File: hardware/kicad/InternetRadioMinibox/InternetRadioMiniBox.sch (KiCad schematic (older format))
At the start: 51 parts, among them IC1 ESP8266, IC2 ATMEGA328P-P, IC3 23K256, IC4 VS1011e, IC5 LM386, M1 TSR1-2433, M2 TSR1-2433, M3 TSR1-2433, P1 CONN_01X02, P2 CONN_01X03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

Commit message: Changed connection to variable capacitor.
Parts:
- removed P2: CONN_01X03, Connect:PINHEAD1-3, symbol CONN_01X03
- added P?: CONN_01X02, symbol CONN_01X02
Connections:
- wire segments 217 -> 256
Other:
- note added: "To 0-135pF Rotary \nVariable Capacitor."
- note removed: "To 0-135pF Rotary \nVariable Capacitor. \nCase connected \nto ground."
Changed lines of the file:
@@
 $EndComp
 Text Notes 15350 2950 0    39   ~ 0
-To 0-135pF Rotary \nVariable Capacitor. \nCase connected \nto ground.
+To 0-135pF Rotary \nVariable Capacitor.
 $Comp
 L GND #PWR013
@@
 $EndComp
 $Comp
-L CONN_01X03 P2
-U 1 1 58D6D6E2
-P 15550 3300
-F 0 "P2" H 15550 3500 50  0000 C CNN
-F 1 "CONN_01X03" V 15650 3300 50  0000 C CNN
-F 2 "Connect:PINHEAD1-3" H 15550 3300 50  0001 C CNN
-F 3 "" H 15550 3300 50  0000 C CNN
-	1    15550 3300
-	1    0    0    -1
-$EndComp
-$Comp
 L CONN_01X02 P3
 U 1 1 58D7596B
@@
 	4400 2800 5300 2800
 Wire Wire Line
-	1350 8300 2800 8300
+	1350 8300 2400 8300
+Wire Wire Line
+	2400 8300 2800 8300
 Wire Wire Line
 	3300 8600 3300 8700
@@
 	6750 2200 4400 2200
 Wire Wire Line
-	6550 8500 8200 8500
+	6550 8500 7750 8500
+Wire Wire Line
+	7750 8500 8200 8500
 Wire Wire Line
 	6550 8500 6550 2500
@@
 	6350 3000 6350 8400
 Wire Wire Line
-	4400 2400 5900 2400
+	4400 2400 4500 2400
+Wire Wire Line
+	4500 2400 5900 2400
 Wire Wire Line
 	4500 4500 4500 2400
 Wire Wire Line
-	3500 4500 4500 4500
+	3500 4500 3600 4500
+Wire Wire Line
+	3600 4500 4500 4500
 Wire Wire Line
 	3500 4500 3500 4600
 Connection ~ 4500 2400
 Wire Wire Line
-	3500 5100 3500 5500
-Wire Wire Line
-	2350 1450 2350 4600
-Wire Wire Line
-	2350 5100 2350 5500
+	3500 5100 3500 5150
+Wire Wire Line
+	3500 5150 3500 5500
+Wire Wire Line
+	2350 1450 2350 2600
+Wire Wire Line
+	2350 2600 2350 4500
+Wire Wire Line
+	2350 4500 2350 4600
+Wire Wire Line
+	2350 5100 2350 5150
+Wire Wire Line
+	2350 5150 2350 5500
 Wire Wire Line
 	10200 2200 12350 2200
 Wire Wire Line
-	12350 2200 12350 2450
+	12350 2200 12350 2400
+Wire Wire Line
+	12350 2400 12350 2450
 Wire Wire Line
 	12350 2400 12200 2400
@@
 	11700 2400 11900 2400
 Wire Wire Line
-	11700 2300 11700 2450
+	11700 2300 11700 2400
+Wire Wire Line
+	11700 2400 11700 2450
 Connection ~ 11700 2400
 Connection ~ 12350 2400
@@
 	12350 2750 12350 2750
 Wire Wire Line
-	7600 950  7600 2550
+	7600 950  7600 1100
+Wire Wire Line
+	7600 1100 7600 1600
+Wire Wire Line
+	7600 1600 7600 2550
 Wire Wire Line
 	8300 3900 7600 3900
 Wire Wire Line
-	7600 2850 7600 4100
+	7600 2850 7600 3900
+Wire Wire Line
+	7600 3900 7600 4100
 Connection ~ 7600 3900
 Wire Wire Line
 	8300 3800 8050 3800
 Wire Wire Line
-	8050 2850 8050 4100
-Wire Wire Line
-	8050 1100 8050 2550
+	8050 2850 8050 3800
+Wire Wire Line
+	8050 3800 8050 4100
+Wire Wire Line
+	8050 1100 8050 1900
+Wire Wire Line
+	8050 1900 8050 2550
 Connection ~ 8050 3800
 Wire Wire Line
 	10400 1500 10400 3050
 Wire Wire Line
-	10200 3050 10950 3050
+	10200 3050 10400 3050
+Wire Wire Line
+	10400 3050 10950 3050
 Wire Wire Line
 	10200 2300 11700 2300
@@
 	11250 2950 11250 3300
 Wire Wire Line
-	11250 3300 15350 3300
+	11250 3300 15050 3300
+Wire Wire Line
+	15050 3300 15350 3300
 Wire Wire Line
 	10200 2850 11350 2850
@@
 	10200 3500 10950 3500
 Wire Wire Line
-	11550 3500 11550 4100
+	11550 3500 11550 3800
+Wire Wire Line
+	11550 3800 11550 4100
 Connection ~ 11550 3800
 Connection ~ 10400 3050
@@
 	4400 2300 6100 2300
 Wire Bus Line
-	1150 6300 14650 6300
+	1150 6300 1250 6300
+Wire Bus Line
+	1250 6300 1400 6300
+Wire Bus Line
+	1400 6300 1550 6300
+Wire Bus Line
+	1550 6300 1700 6300
+Wire Bus Line
+	1700 6300 5200 6300
+Wire Bus Line
+	5200 6300 5400 6300
+Wire Bus Line
+	5400 6300 5600 6300
+Wire Bus Line
+	5600 6300 5800 6300
+Wire Bus Line
+	5800 6300 6000 6300
+Wire Bus Line
+	6000 6300 6200 6300
+Wire Bus Line
+	6200 6300 7250 6300
+Wire Bus Line
+	7250 6300 7350 6300
+Wire Bus Line
+	7350 6300 7450 6300
+Wire Bus Line
+	7450 6300 7550 6300
+Wire Bus Line
+	7550 6300 13100 6300
+Wire Bus Line
+	13100 6300 13300 6300
+Wire Bus Line
+	13300 6300 13500 6300
+Wire Bus Line
+	13500 6300 13700 6300
+Wire Bus Line
+	13700 6300 14650 6300
 Wire Wire Line
 	5100 2900 5100 6200
@@
 Wire Wire Line
 	1800 8000 1800 6400
-Connection ~ 15050 3700
 Wire Bus Line
 	13100 6300 13050 6300
@@
 Connection ~ 2700 7050
 Wire Wire Line
-	2400 7050 3300 7050
+	2400 7050 2700 7050
+Wire Wire Line
+	2700 7050 3300 7050
 Wire Wire Line
 	3700 3600 3700 3550
 Wire Wire Line
-	3300 7000 3300 7550
+	3300 7000 3300 7050
+Wire Wire Line
+	3300 7050 3300 7550
 Wire Wire Line
 	8050 1900 8300 1900
 Wire Wire Line
-	7600 1100 10400 1100
+	7600 1100 8050 1100
+Wire Wire Line
+	8050 1100 10400 1100
 Connection ~ 7600 1100
 Connection ~ 8050 1100
@@
 	8600 9400 8600 9500
 Wire Wire Line
-	8600 9500 8800 9500
-Wire Wire Line
-	8700 9400 8700 9600
+	8600 9500 8700 9500
+Wire Wire Line
+	8700 9500 8800 9500
+Wire Wire Line
+	8700 9400 8700 9500
+Wire Wire Line
+	8700 9500 8700 9600
 Wire Wire Line
 	8800 9500 8800 9400
@@
 	8950 9400 8950 9500
 Wire Wire Line
-	8950 9500 9150 9500
-Wire Wire Line
-	9050 9400 9050 9600
+	8950 9500 9050 9500
+Wire Wire Line
+	9050 9500 9150 9500
+Wire Wire Line
+	9050 9400 9050 9500
+Wire Wire Line
+	9050 9500 9050 9600
 Connection ~ 9050 9500
 Wire Wire Line
@@
 	8600 7200 8600 7100
 Wire Wire Line
-	8600 7100 8800 7100
-Wire Wire Line
-	8700 6450 8700 7200
+	8600 7100 8700 7100
+Wire Wire Line
+	8700 7100 8800 7100
+Wire Wire Line
+	8700 6450 8700 7100
+Wire Wire Line
+	8700 7100 8700 7200
 Connection ~ 8700 7100
 Wire Wire Line
@@
 	6250 10700 6250 10800
 Wire Wire Line
-	9050 6450 9050 7200
+	9050 6450 9050 7100
+Wire Wire Line
+	9050 7100 9050 7200
 Wire Wire Line
 	8950 7200 8950 7100
@@
 	10200 7150 10200 7350
 Wire Wire Line
-	10150 7150 10400 7150
-Wire Wire Line
-	10750 7150 10750 7950
+	10150 7150 10200 7150
+Wire Wire Line
+	10200 7150 10400 7150
+Wire Wire Line
+	10750 7150 10750 7850
+Wire Wire Line
+	10750 7850 10750 7950
 Wire Wire Line
 	10200 7850 10200 7650
@@
 	10000 9200 10000 9250
 Wire Wire Line
-	10000 9250 10600 9250
-Wire Wire Line
-	10200 9200 10200 9300
+	10000 9250 10200 9250
+Wire Wire Line
+	10200 9250 10400 9250
+Wire Wire Line
+	10400 9250 10600 9250
+Wire Wire Line
+	10200 9200 10200 9250
+Wire Wire Line
+	10200 9250 10200 9300
 Connection ~ 10200 9250
 Wire Wire Line
@@
 	2850 10150 2650 10150
 Wire Wire Line
-	1150 10150 1450 10150
-Wire Wire Line
-	2050 10700 2050 10800
+	1150 10150 1400 10150
+Wire Wire Line
+	1400 10150 1450 10150
+Wire Wire Line
+	2050 10700 2050 10750
+Wire Wire Line
+	2050 10750 2050 10800
 Wire Wire Line
 	3250 10150 3350 10150
@@
 Connection ~ 2350 2600
 Wire Wire Line
-	13400 8500 13400 8650
+	13400 8500 13400 8600
+Wire Wire Line
+	13400 8600 13400 8650
 Wire Wire Line
 	13200 8300 13200 8600
@@
 	13400 7650 13400 7900
 Wire Wire Line
-	13800 8200 14100 8200
+	13800 8200 14000 8200
+Wire Wire Line
+	14000 8200 14100 8200
 Wire Wire Line
 	14000 8500 14000 8200
@@
 	14000 9100 14000 9150
 Wire Wire Line
-	13000 8100 13200 8100
-Wire Wire Line
-	13050 8100 13050 8600
+	13000 8100 13050 8100
+Wire Wire Line
+	13050 8100 13200 8100
+Wire Wire Line
+	13050 8100 13050 8450
+Wire Wire Line
+	13050 8450 13050 8600
 Connection ~ 13050 8100
 Connection ~ 13050 8450
@@
 	10700 7150 10750 7150
 Wire Wire Line
-	9650 7850 10400 7850
+	9650 7850 10200 7850
+Wire Wire Line
+	10200 7850 10400 7850
 Connection ~ 10200 7850
 Wire Wire Line
@@
 ISP for AVR (Optional)
 Wire Wire Line
-	15350 3400 15350 3700
-Wire Wire Line
-	15350 3700 15050 3700
-Wire Wire Line
-	15050 3650 15050 3800
+	15050 3650 15050 3700
+Wire Wire Line
+	15050 3700 15050 3800
 Text Notes 3950 1750 0    60   ~ 0
 Main Processor
@@
 ESP8266 Board has 12K pullups \non GPIO0 and CHIP-EN
 NoConn ~ 3000 2700
+$Comp
+L CONN_01X02 P?
+U 1 1 58F755C2
+P 15550 3250
+F 0 "P?" H 15550 3400 50  0000 C CNN
+F 1 "CONN_01X02" V 15650 3250 50  0000 C CNN
+F 2 "" H 15550 3250 50  0000 C CNN
+F 3 "" H 15550 3250 50  0000 C CNN
+	1    15550 3250
+	1    0    0    -1
+$EndComp
 $EndSCHEMATC

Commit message: Small changes to the schematic.
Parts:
- C13: footprint (none) -> Capacitors_SMD:C_0805_HandSoldering
- R17, R18, R19, R20: footprint (none) -> Resistors_SMD:R_0805_HandSoldering
- gave numbers to parts that had none: 2
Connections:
- wire segments 256 -> 215
- no-connect marks 18 -> 19

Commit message: KiCAD update of library caches.
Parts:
- D1, D2: symbol LED -> LED-RESCUE-InternetRadioMiniBox
- IC5: symbol LM386 -> LM386-RESCUE-InternetRadioMiniBox
- SW1, SW2: symbol SW_PUSH_SMALL -> SW_PUSH_SMALL-RESCUE-InternetRadioMiniBox
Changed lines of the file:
@@
 $EndComp
 $Comp
-L LED D2
+L LED-RESCUE-InternetRadioMiniBox D2
 U 1 1 58AB9582
 P 11100 3800
@@
 $EndComp
 $Comp
-L LED D1
+L LED-RESCUE-InternetRadioMiniBox D1
 U 1 1 58AB95F9
 P 11100 3500
@@
 $EndComp
 $Comp
-L SW_PUSH_SMALL SW1
+L SW_PUSH_SMALL-RESCUE-InternetRadioMiniBox SW1
 U 1 1 58CEFEA7
 P 2400 4850
@@
 $EndComp
 $Comp
-L SW_PUSH_SMALL SW2
+L SW_PUSH_SMALL-RESCUE-InternetRadioMiniBox SW2
 U 1 1 58CF00A3
 P 3550 4850
@@
 $EndComp
 $Comp
-L LM386 IC5
+L LM386-RESCUE-InternetRadioMiniBox IC5
 U 1 1 58D2B6DF
 P 13500 8200

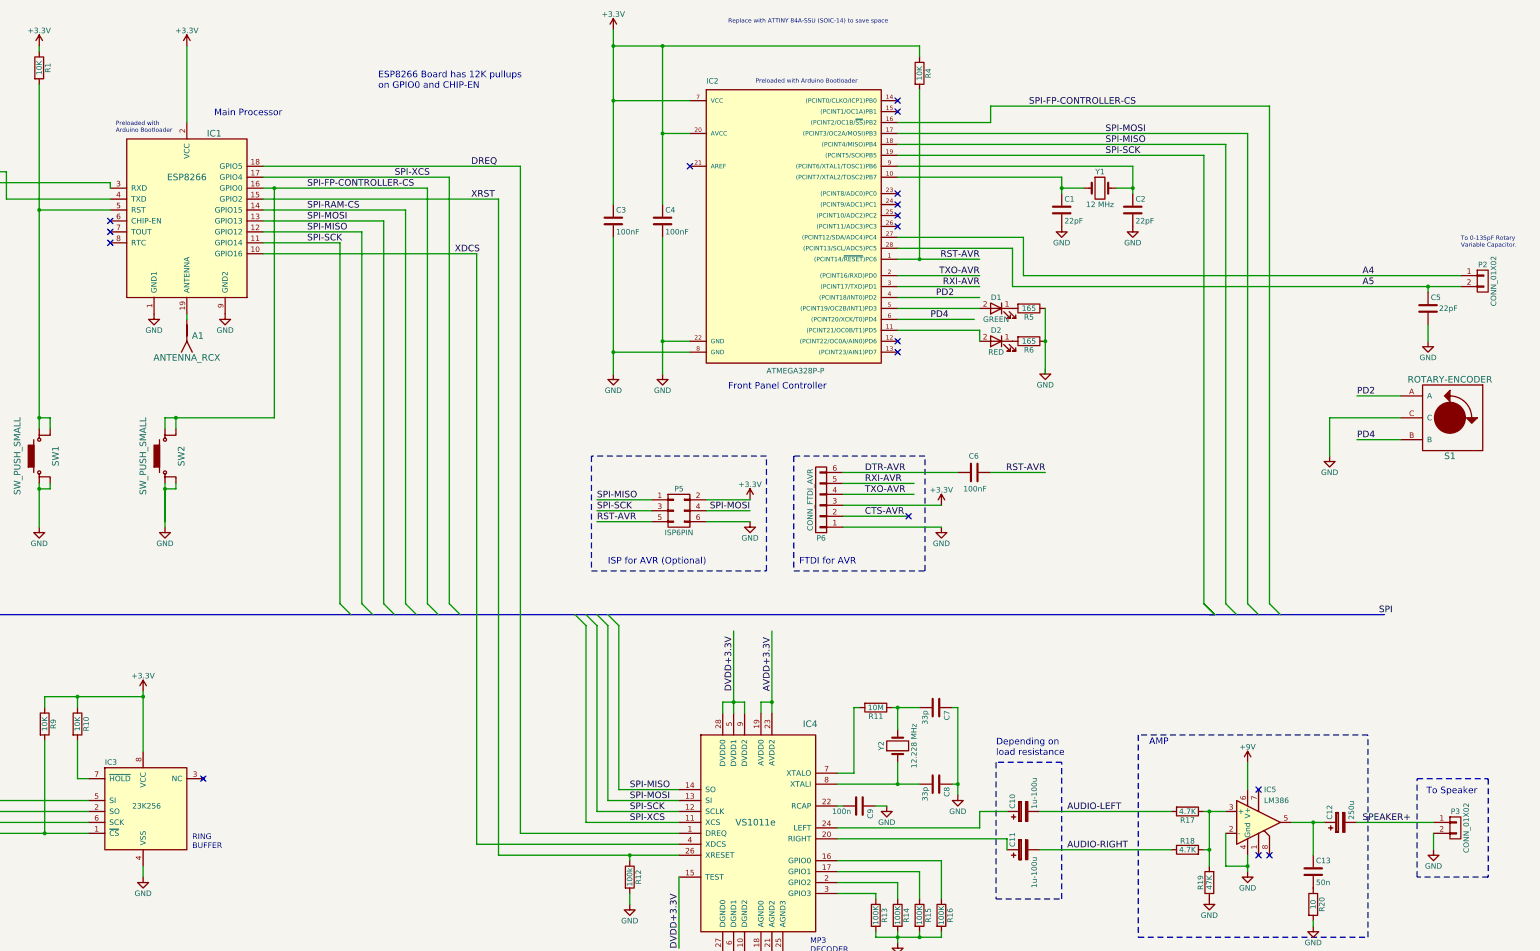
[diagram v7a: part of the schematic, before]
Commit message: Added decoupling capacitors.
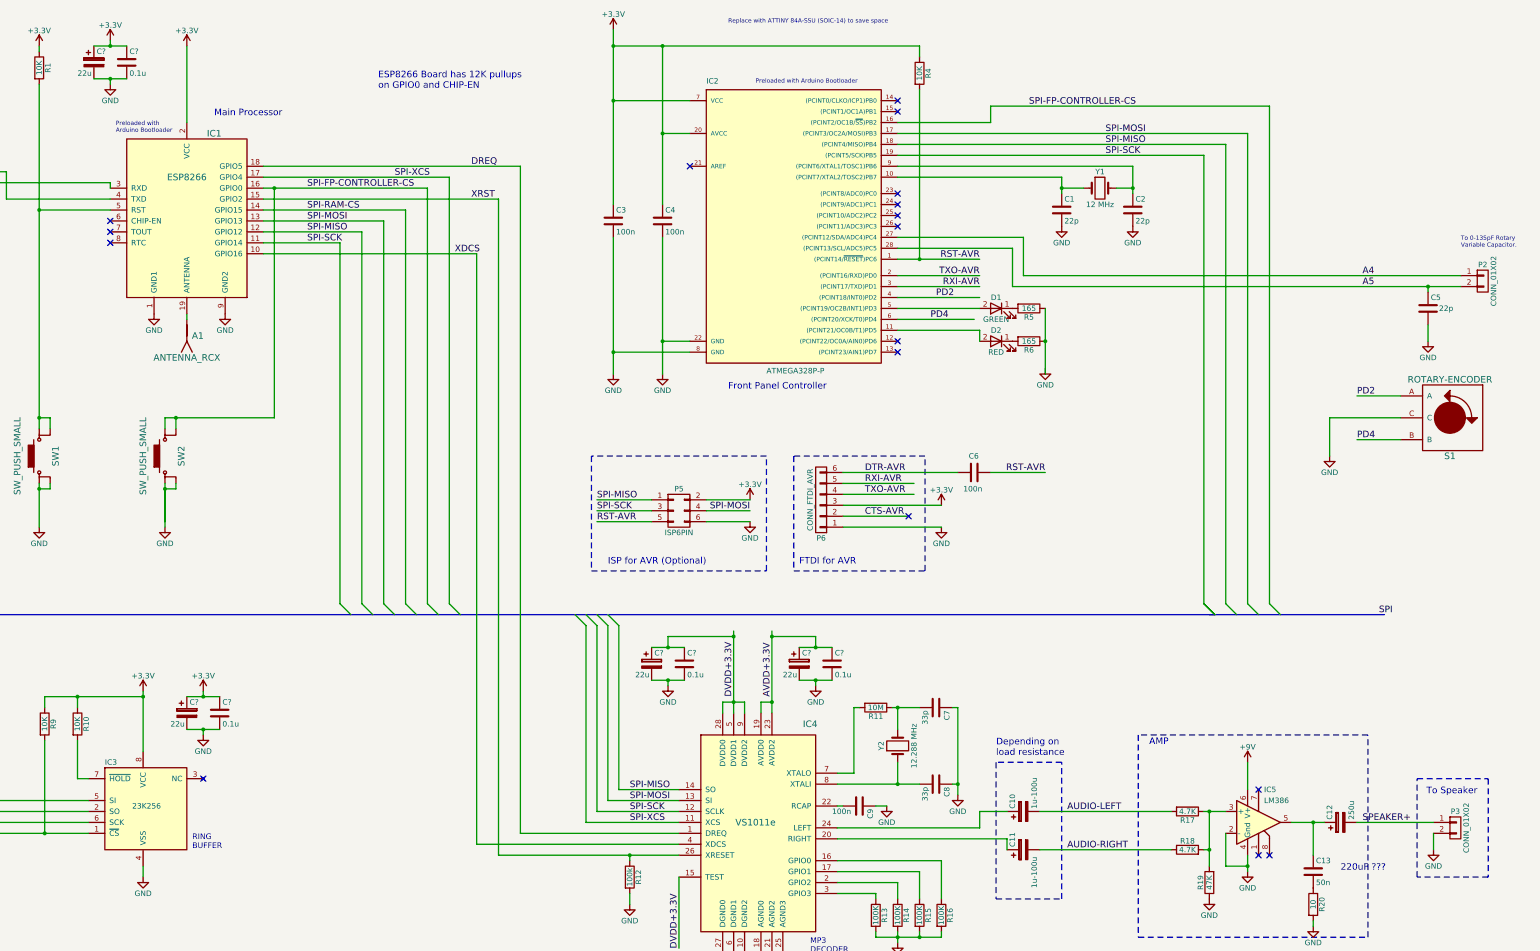
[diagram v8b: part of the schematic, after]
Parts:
- added C? (x4): 22u, symbol CP
- added C? (x4): 0.1u, symbol C
- C1, C2, C5: value 22pF -> 22p
- C3, C4, C6: value 100nF -> 100n
- Y2: value 12.228 MHz -> 12.288 MHz
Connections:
- wire segments 215 -> 233
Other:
- note added: "220uF ???"
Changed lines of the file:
@@
 P 11700 2600
 F 0 "C1" H 11725 2700 50  0000 L CNN
-F 1 "22pF" H 11725 2500 50  0000 L CNN
+F 1 "22p" H 11725 2500 50  0000 L CNN
 F 2 "Capacitors_SMD:C_0805_HandSoldering" H 11738 2450 50  0001 C CNN
 F 3 "" H 11700 2600 50  0000 C CNN
@@
 P 12350 2600
 F 0 "C2" H 12375 2700 50  0000 L CNN
-F 1 "22pF" H 12375 2500 50  0000 L CNN
+F 1 "22p" H 12375 2500 50  0000 L CNN
 F 2 "Capacitors_SMD:C_0805_HandSoldering" H 12388 2450 50  0001 C CNN
 F 3 "" H 12350 2600 50  0000 C CNN
@@
 P 7600 2700
 F 0 "C3" H 7625 2800 50  0000 L CNN
-F 1 "100nF" H 7625 2600 50  0000 L CNN
+F 1 "100n" H 7625 2600 50  0000 L CNN
 F 2 "Capacitors_SMD:C_0805_HandSoldering" H 7638 2550 50  0001 C CNN
 F 3 "" H 7600 2700 50  0000 C CNN
@@
 P 8050 2700
 F 0 "C4" H 8075 2800 50  0000 L CNN
-F 1 "100nF" H 8075 2600 50  0000 L CNN
+F 1 "100n" H 8075 2600 50  0000 L CNN
 F 2 "Capacitors_SMD:C_0805_HandSoldering" H 8088 2550 50  0001 C CNN
 F 3 "" H 8050 2700 50  0000 C CNN
@@
 P 15050 3500
 F 0 "C5" H 15075 3600 50  0000 L CNN
-F 1 "22pF" H 15150 3500 50  0000 L CNN
+F 1 "22p" H 15150 3500 50  0000 L CNN
 F 2 "Capacitors_SMD:C_0805_HandSoldering" H 15088 3350 50  0001 C CNN
 F 3 "" H 15050 3500 50  0000 C CNN
@@
 P 10900 5000
 F 0 "C6" V 10750 4950 50  0000 L CNN
-F 1 "100nF" V 11050 4900 50  0000 L CNN
+F 1 "100n" V 11050 4900 50  0000 L CNN
 F 2 "Capacitors_SMD:C_0805_HandSoldering" H 10938 4850 50  0001 C CNN
 F 3 "" H 10900 5000 50  0000 C CNN
@@
 P 10200 7500
 F 0 "Y2" H 10200 7650 50  0000 C CNN
-F 1 "12.228 MHz" H 10200 7350 50  0000 C CNN
+F 1 "12.288 MHz" H 10200 7350 50  0000 C CNN
 F 2 "" H 10200 7500 50  0001 C CNN
 F 3 "" H 10200 7500 50  0000 C CNN
@@
 Wire Wire Line
 	1300 2650 1800 2650
-Text Label 8700 7000 1    60   ~ 0
+Text Label 8700 7050 1    60   ~ 0
 DVDD+3.3V
-Text Label 9050 7000 1    60   ~ 0
+Text Label 9050 7050 1    60   ~ 0
 AVDD+3.3V
 Text Label 7500 10150 2    60   ~ 0
@@
 $EndComp
 NoConn ~ 10200 2450
+Text Notes 14250 8650 0    60   ~ 0
+220uF ???
+$Comp
+L CP C?
+U 1 1 5905CE91
+P 2850 1250
+F 0 "C?" H 2875 1350 50  0000 L CNN
+F 1 "22u" H 2700 1150 50  0000 L CNN
+F 2 "" H 2888 1100 50  0000 C CNN
+F 3 "" H 2850 1250 50  0000 C CNN
+	1    2850 1250
+	1    0    0    -1
+$EndComp
+$Comp
+L C C?
+U 1 1 5905CF1A
+P 3150 1250
+F 0 "C?" H 3175 1350 50  0000 L CNN
+F 1 "0.1u" H 3175 1150 50  0000 L CNN
+F 2 "" H 3188 1100 50  0000 C CNN
+F 3 "" H 3150 1250 50  0000 C CNN
+	1    3150 1250
+	1    0    0    -1
+$EndComp
+Wire Wire Line
+	2850 1100 3150 1100
+Wire Wire Line
+	2850 1400 3150 1400
+$Comp
+L +3.3V #PWR?
+U 1 1 5905E727
+P 3000 1050
+F 0 "#PWR?" H 3000 900 50  0001 C CNN
+F 1 "+3.3V" H 3000 1190 50  0000 C CNN
+F 2 "" H 3000 1050 50  0000 C CNN
+F 3 "" H 3000 1050 50  0000 C CNN
+	1    3000 1050
+	1    0    0    -1
+$EndComp
+$Comp
+L GND #PWR?
+U 1 1 5905E7A5
+P 3000 1450
+F 0 "#PWR?" H 3000 1200 50  0001 C CNN
+F 1 "GND" H 3000 1300 50  0000 C CNN
+F 2 "" H 3000 1450 50  0000 C CNN
+F 3 "" H 3000 1450 50  0000 C CNN
+	1    3000 1450
+	1    0    0    -1
+$EndComp
+Wire Wire Line
+	3000 1050 3000 1100
+Connection ~ 3000 1100
+Wire Wire Line
+	3000 1450 3000 1400
+Connection ~ 3000 1400
+$Comp
+L CP C?
+U 1 1 59060BA4
+P 3700 7200
+F 0 "C?" H 3725 7300 50  0000 L CNN
+F 1 "22u" H 3550 7100 50  0000 L CNN
+F 2 "" H 3738 7050 50  0000 C CNN
+F 3 "" H 3700 7200 50  0000 C CNN
+	1    3700 7200
+	1    0    0    -1
+$EndComp
+$Comp
+L C C?
+U 1 1 59060BAA
+P 4000 7200
+F 0 "C?" H 4025 7300 50  0000 L CNN
+F 1 "0.1u" H 4025 7100 50  0000 L CNN
+F 2 "" H 4038 7050 50  0000 C CNN
+F 3 "" H 4000 7200 50  0000 C CNN
+	1    4000 7200
+	1    0    0    -1
+$EndComp
+Wire Wire Line
+	3700 7050 4000 7050
+Wire Wire Line
+	3700 7350 4000 7350
+$Comp
+L +3.3V #PWR?
+U 1 1 59060BB4
+P 3850 7000
+F 0 "#PWR?" H 3850 6850 50  0001 C CNN
+F 1 "+3.3V" H 3850 7140 50  0000 C CNN
+F 2 "" H 3850 7000 50  0000 C CNN
+F 3 "" H 3850 7000 50  0000 C CNN
+	1    3850 7000
+	1    0    0    -1
+$EndComp
+$Comp
+L GND #PWR?
+U 1 1 59060BBA
+P 3850 7400
+F 0 "#PWR?" H 3850 7150 50  0001 C CNN
+F 1 "GND" H 3850 7250 50  0000 C CNN
+F 2 "" H 3850 7400 50  0000 C CNN
+F 3 "" H 3850 7400 50  0000 C CNN
+	1    3850 7400
+	1    0    0    -1
+$EndComp
+Wire Wire Line
+	3850 7000 3850 7050
+Connection ~ 3850 7050
+Wire Wire Line
+	3850 7400 3850 7350
+Connection ~ 3850 7350
+$Comp
+L CP C?
+U 1 1 59062737
+P 7950 6750
+F 0 "C?" H 7975 6850 50  0000 L CNN
+F 1 "22u" H 7800 6650 50  0000 L CNN
+F 2 "" H 7988 6600 50  0000 C CNN
+F 3 "" H 7950 6750 50  0000 C CNN
+	1    7950 6750
+	1    0    0    -1
+$EndComp
+$Comp
+L C C?
+U 1 1 5906273D
+P 8250 6750
+F 0 "C?" H 8275 6850 50  0000 L CNN
+F 1 "0.1u" H 8275 6650 50  0000 L CNN
+F 2 "" H 8288 6600 50  0000 C CNN
+F 3 "" H 8250 6750 50  0000 C CNN
+	1    8250 6750
+	1    0    0    -1
+$EndComp
+Wire Wire Line
+	7950 6600 8250 6600
+Wire Wire Line
+	7950 6900 8250 6900
+$Comp
+L GND #PWR?
+U 1 1 5906274D
+P 8100 6950
+F 0 "#PWR?" H 8100 6700 50  0001 C CNN
+F 1 "GND" H 8100 6800 50  0000 C CNN
+F 2 "" H 8100 6950 50  0000 C CNN
+F 3 "" H 8100 6950 50  0000 C CNN
+	1    8100 6950
+	1    0    0    -1
+$EndComp
+Wire Wire Line
+	8100 6500 8100 6600
+Connection ~ 8100 6600
+Wire Wire Line
+	8100 6950 8100 6900
+Connection ~ 8100 6900
+$Comp
+L CP C?
+U 1 1 59062D0E
+P 9300 6750
+F 0 "C?" H 9325 6850 50  0000 L CNN
+F 1 "22u" H 9150 6650 50  0000 L CNN
+F 2 "" H 9338 6600 50  0000 C CNN
+F 3 "" H 9300 6750 50  0000 C CNN
+	1    9300 6750
+	1    0    0    -1
+$EndComp
+$Comp
+L C C?
+U 1 1 59062D14
+P 9600 6750
+F 0 "C?" H 9625 6850 50  0000 L CNN
+F 1 "0.1u" H 9625 6650 50  0000 L CNN
+F 2 "" H 9638 6600 50  0000 C CNN
+F 3 "" H 9600 6750 50  0000 C CNN
+	1    9600 6750
+	1    0    0    -1
+$EndComp
+Wire Wire Line
+	9300 6600 9600 6600
+Wire Wire Line
+	9300 6900 9600 6900
+$Comp
+L GND #PWR?
+U 1 1 59062D24
+P 9450 6950
+F 0 "#PWR?" H 9450 6700 50  0001 C CNN
+F 1 "GND" H 9450 6800 50  0000 C CNN
+F 2 "" H 9450 6950 50  0000 C CNN
+F 3 "" H 9450 6950 50  0000 C CNN
+	1    9450 6950
+	1    0    0    -1
+$EndComp
+Connection ~ 9450 6600
+Wire Wire Line
+	9450 6950 9450 6900
+Connection ~ 9450 6900
+Wire Wire Line
+	8100 6500 8700 6500
+Connection ~ 8700 6500
+Wire Wire Line
+	9450 6600 9450 6500
+Wire Wire Line
+	9450 6500 9050 6500
+Connection ~ 9050 6500
 $EndSCHEMATC
